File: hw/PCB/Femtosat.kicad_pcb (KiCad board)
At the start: 2 copper layers, 83.8 x 34 mm, 35 parts, among them J1 USB_B_Micro, J2 Programmer, J3 U.FL, J4 Battery, J5 Micro_SD_Card_Det, SW1 Reset_push, U0 SAMD21E, U1 AP7215-33YG-13, U2 AV4524, U3 RFM69HCW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

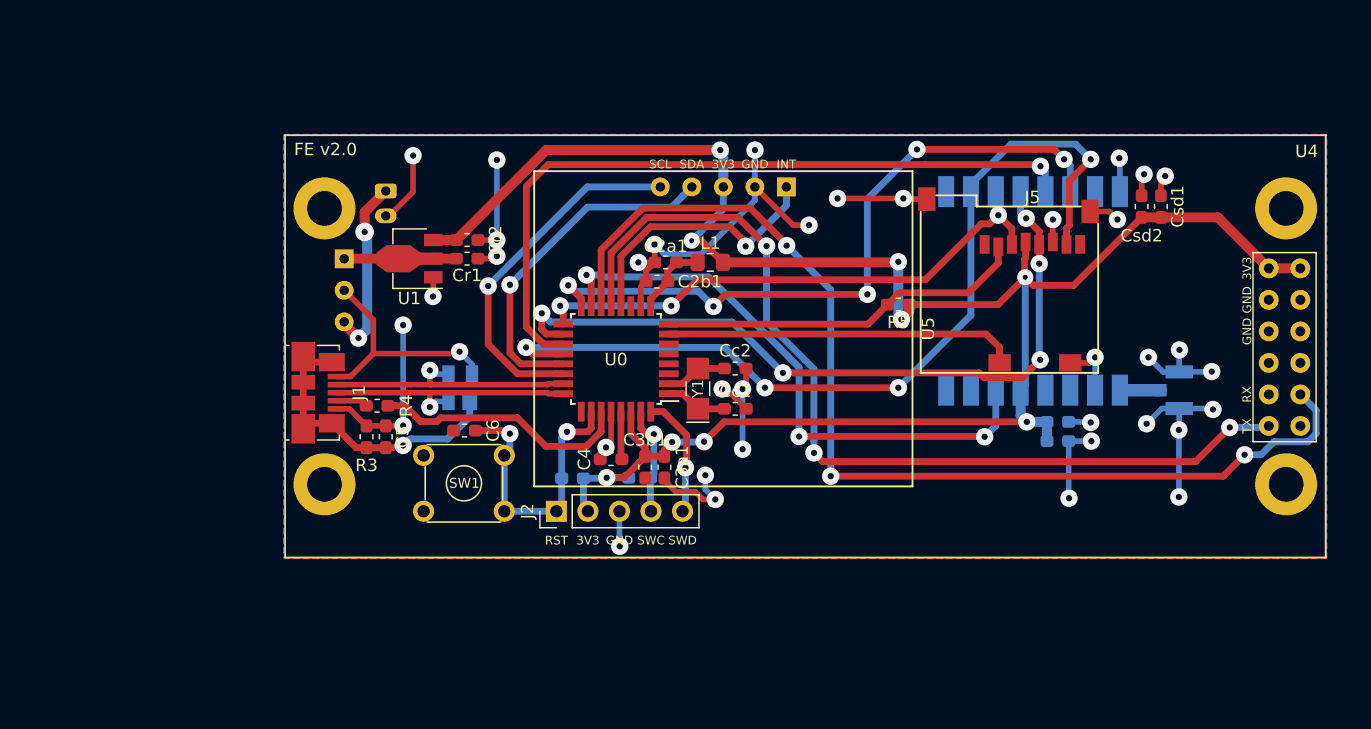
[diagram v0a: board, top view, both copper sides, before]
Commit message: Changed the pin order of the pin header to connect the femto-satellite to the GPS TRH-G2. Now this connector has a battery voltage input for a future EPS board.
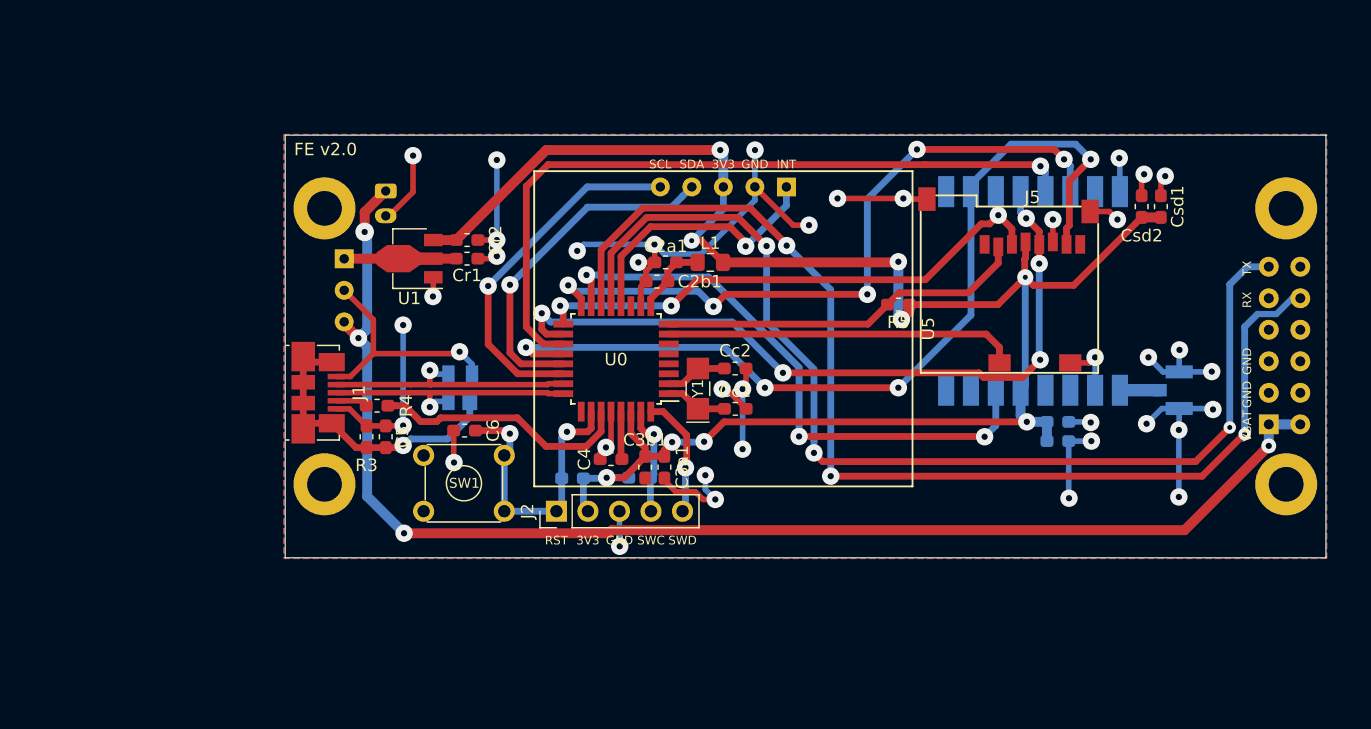
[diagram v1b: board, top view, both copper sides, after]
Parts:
- U4: moved to B.Cu
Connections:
- U4 pad 1: +3V3 -> /VBAT
- U4 pad 2: +3V3 -> /VBAT
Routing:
- net /VBAT: track 14.7 -> 109.0 mm, vias 2 -> 4
- net +3V3: track 160.2 -> 147.2 mm
- net /TX: track 75.3 -> 87.4 mm
- net GND: track 132.5 -> 141.5 mm, vias 36 -> 38
- net /RX: track 86.4 -> 91.1 mm
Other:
- board text added: "VBAT"

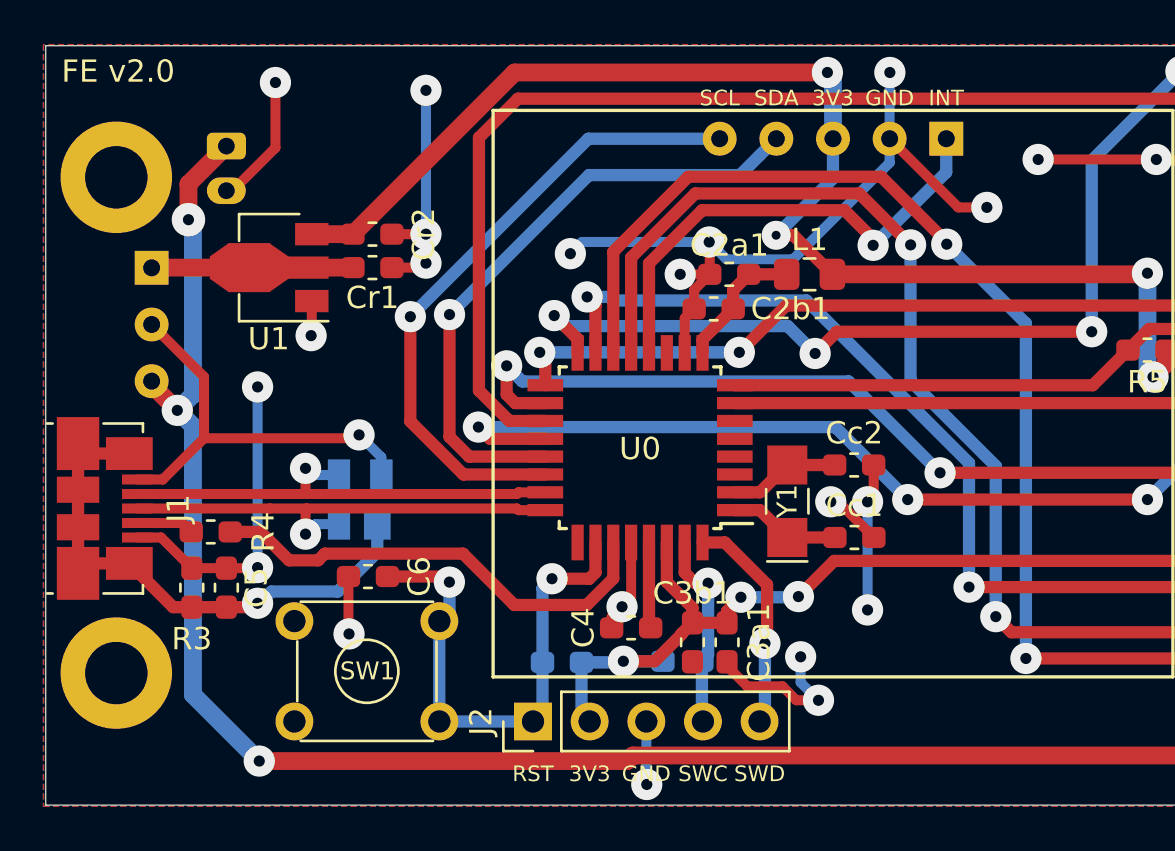
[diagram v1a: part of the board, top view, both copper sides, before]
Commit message: Increased the size of the pad and the drill of the interrupter.
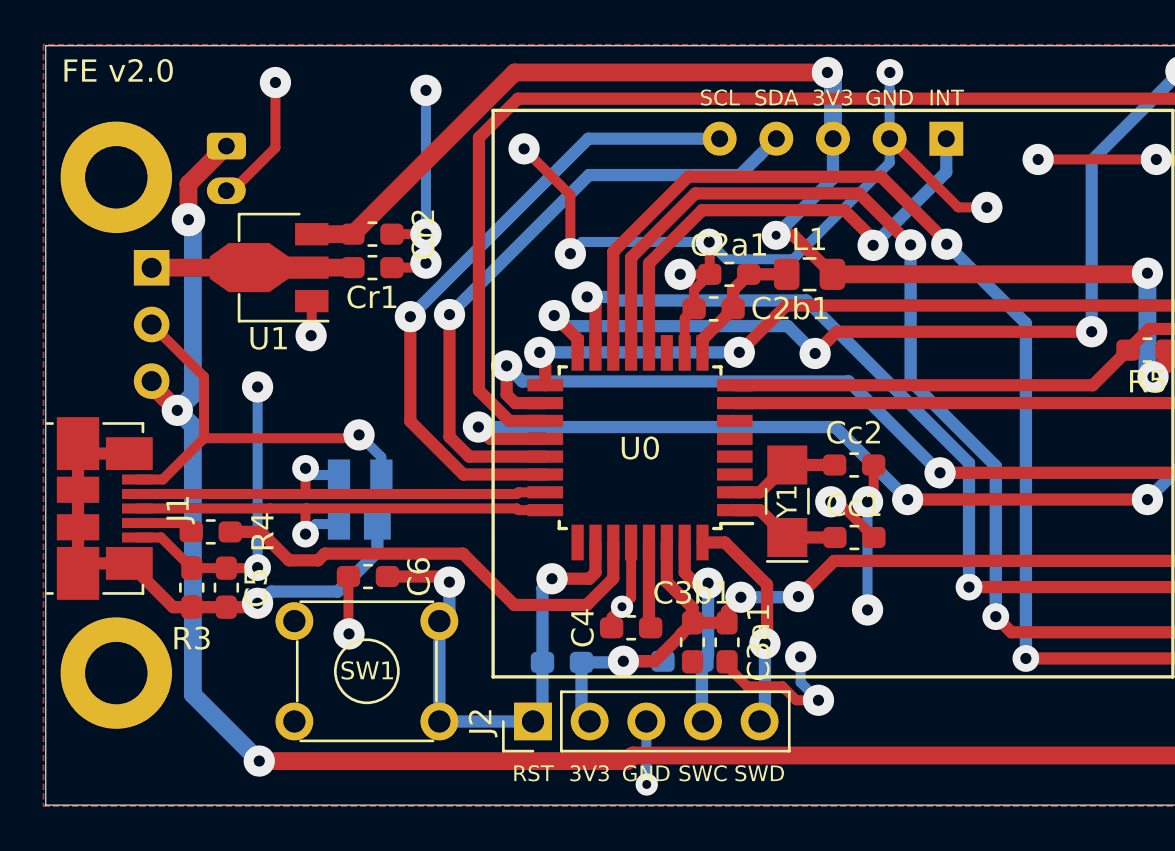
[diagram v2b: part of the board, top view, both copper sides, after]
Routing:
- net GND: track 141.5 -> 147.0 mm, vias 38 -> 39

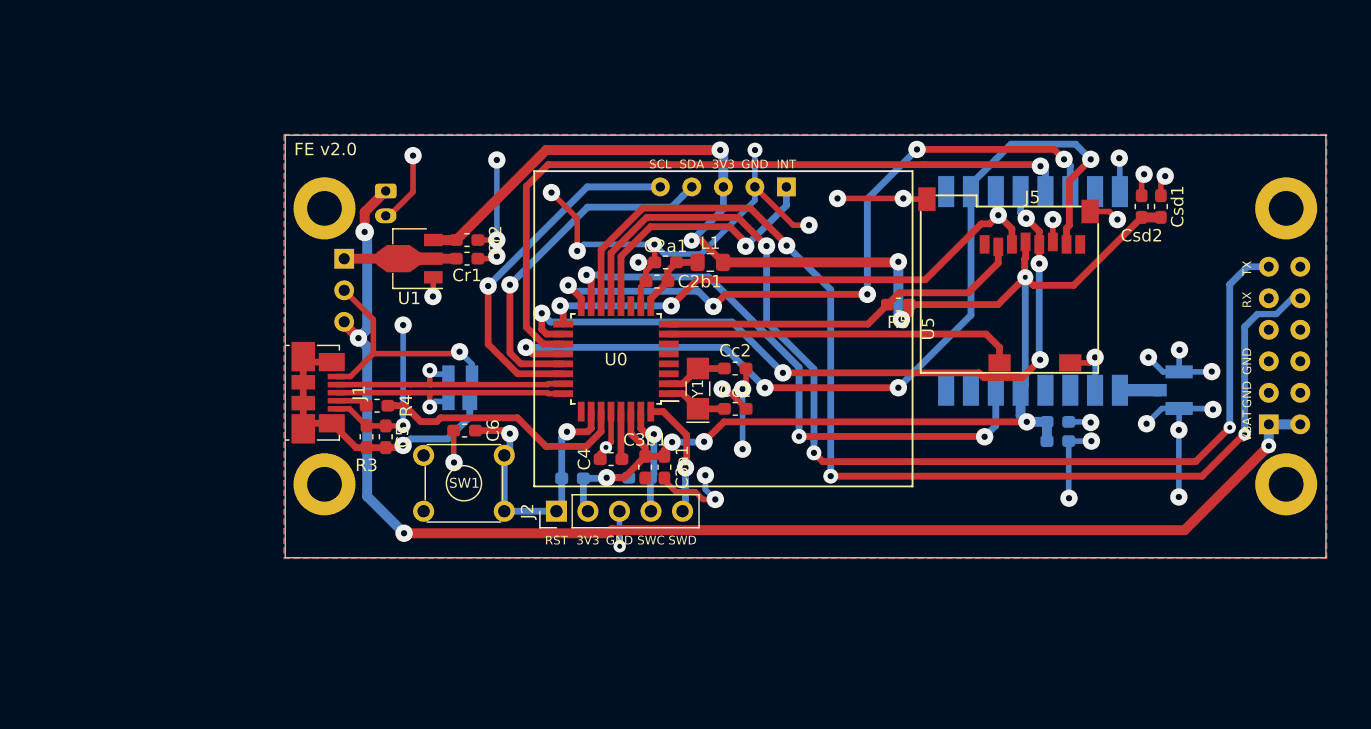
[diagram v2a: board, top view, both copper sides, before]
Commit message: New design of the femto-satellite. Deleted UHF transceiver and added another one in S band. Changed the magnetometer. Added more space.
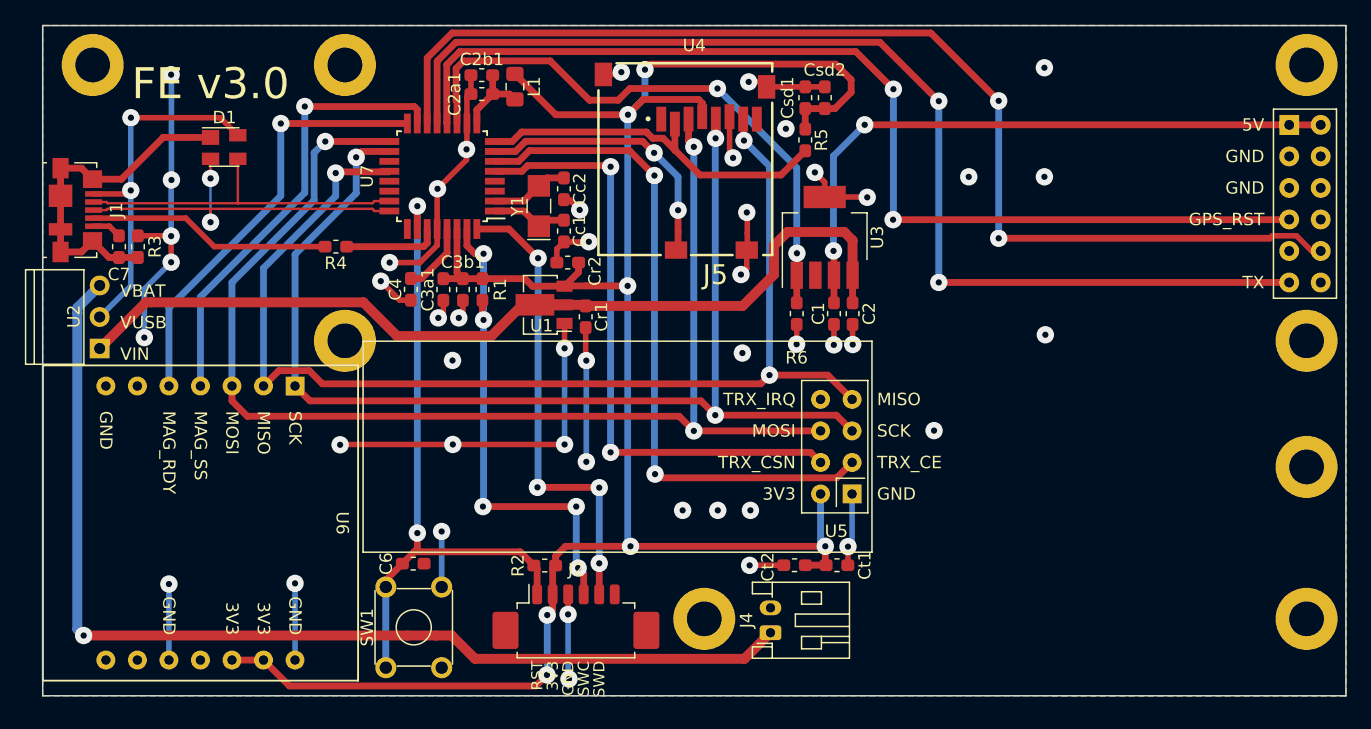
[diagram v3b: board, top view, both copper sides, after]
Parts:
- removed C5: 4.7nF, Capacitor_SMD:C_0603_1608Metric_Pad1.05x0.95mm_HandSolder
- removed J3: U.FL, Connector_Coaxial:U.FL_Hirose_U.FL-R-SMT-1_Vertical
- removed U0: SAMD21E, Package_QFP:TQFP-32_7x7mm_P0.8mm
- added C1: 1uF, Capacitor_SMD:C_0603_1608Metric_Pad1.05x0.95mm_HandSolder, F.Cu at (131.6, 52.7)
- added C2: 1uF, Capacitor_SMD:C_0603_1608Metric_Pad1.05x0.95mm_HandSolder, F.Cu at (130.1, 52.7)
- added C7: 4.7nF, Capacitor_SMD:C_0603_1608Metric_Pad1.05x0.95mm_HandSolder, F.Cu at (72.5, 47.3)
- added R6: 1k, Resistor_SMD:R_0603_1608Metric_Pad1.05x0.95mm_HandSolder, F.Cu at (127.1, 52.7)
- added U6: RM3100, Magnetometer:RM3100, F.Cu at (79.1, 69.5)
- added U7: SAMD21E, Package_QFP:TQFP-32_7x7mm_P0.8mm, F.Cu at (98.5, 41.6)
- Ct1: value 0.1uF -> 100 nF; moved to F.Cu
- Ct2, D1, J4, R1, R2, U2: moved to F.Cu
- J2: footprint Connector_PinHeader_2.54mm:PinHeader_1x05_P2.54mm_Vertical -> Connector_Molex:Molex_PicoBlade_53261-0671_1x06-1MP_P1.25mm_Horizontal
- J5: footprint SD:microSD_socket -> SD:GCT_MEM2061-01-188-00-A_REVA
- U3: value RFM69HCW -> LP38693MP-5.0; footprint Transceptor:RFM69HCW -> Package_TO_SOT_SMD:SOT-223-5; moved to F.Cu
- U4: footprint GPS:TRH-G2 -> GPS:TRH-G2_extended; moved to F.Cu
- U5: value XA1110 -> NRF24L01_Breakout; footprint GPS:XA1110_I2C -> Transceptor:nRF24L01_long
- moved J4 47.2 mm to (125.0, 78.4), turned to 90 degrees
- moved J5 32.1 mm to (118.1, 40.2), turned to 180 degrees
- moved Csd1 30.0 mm to (127.8, 35.3)
- moved D1 27.2 mm to (81.0, 39.3), turned to 0 degrees
- moved Csd2 27.0 mm to (129.4, 35.3)
- moved J1 24.5 mm to (69.0, 44.3)
- moved Ct2 24.2 mm to (126.9, 72.9), turned to 0 degrees
- moved R3 24.0 mm to (74.0, 47.3)
- moved C3a1 22.8 mm to (98.6, 50.7)
- moved C2b1 21.8 mm to (101.7, 33.5)
- moved L1 21.2 mm to (104.4, 34.4), turned to 90 degrees
- moved C4 21.1 mm to (96.0, 50.7), turned to -90 degrees
- moved C3b1 20.5 mm to (100.2, 50.7)
- moved Ct1 20.4 mm to (130.4, 72.9)
- moved C2a1 20.1 mm to (101.7, 35.0)
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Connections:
- SW1 pad 1: GND -> /RESET
- SW1 pad 4: /RESET -> GND
- U3 pad 1: GND -> /GPS_EN
- U3 pad 2: /MISO -> Net-(U3-Pad2)
- U3 pad 3: /MOSI -> /5V
- U3 pad 4: /SCK -> /Power/VIN
- U3 pad 5: /TRX_NSS -> GND
- U4 pad 1: /VBAT -> /5V
- U4 pad 2: /VBAT -> /5V
- U4 pad 7: Net-(U4-Pad7) -> /GPS_RST
- U5 pad 1: /GPS_INT -> GND
- U5 pad 2: GND -> +3V3
- U5 pad 3: +3V3 -> /TRX_CE
- U5 pad 4: /SDA -> /TRX_CSN
- U5 pad 5: /SCL -> /SCK
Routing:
- net /GPS_RST: track 0.00 -> 84.9 mm, vias 0 -> 2
- net /Power/VIN: track 9.04 -> 73.6 mm
- net /TRX_NSS: track 59.3 -> 0.00 mm, vias 1 -> 0
- net /MOSI: track 44.7 -> 102.9 mm
- net /TRX_RST: track 55.6 -> 0.00 mm, vias 5 -> 0
- net /TRX_CE: track 0.00 -> 54.6 mm, vias 0 -> 2
- net /5V: track 0.00 -> 52.1 mm, vias 0 -> 2
- net /TRX_CSN: track 0.00 -> 49.8 mm, vias 0 -> 2
- net /TRX_INT: track 47.5 -> 0.00 mm, vias 3 -> 0
- net /GPS_EN: track 0.00 -> 47.4 mm, vias 0 -> 2
- net /MAG_SS: track 0.00 -> 36.3 mm, vias 0 -> 1
- net /MAG_RDY: track 0.00 -> 35.1 mm, vias 0 -> 1
- net /SCK: track 60.4 -> 94.0 mm, vias 5 -> 3
- net /SWCLK: track 8.93 -> 39.8 mm, vias 1 -> 5
- net /RESET: track 23.7 -> 52.6 mm
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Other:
- board size 83.8 x 34 mm -> 105 x 54 mm
- net class Small added: clearance 0.2, trace_width 0.2, via_dia 1.4, via_drill 0.5
- board text added: "5V"
- board text added: "FE v3.0"
- board text added: "GPS_RST"
- board text added: "MAG_RDY"
- board text added: "MAG_SS"
- board text added: "MISO"
- board text added: "MOSI"
- board text added: "SCK"
- board text added: "TRX_CE"
- board text added: "TRX_CSN"
- board text added: "TRX_IRQ"
- board text added: "VIN"
- board text added: "VUSB"
- board text removed: "+"
- board text removed: "-"
- board text removed: "FE v2.0"
- board text removed: "INT"
- board text removed: "RX"
- board text removed: "SCL"
- board text removed: "SDA"

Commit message: Added a logo to the PCB.
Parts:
- added G***: LOGO, SPEL:SPEL, B.Cu at (155.9, 56.3)
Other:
- board text added: "FE v3.2110"
- board text removed: "FE v3.0"
